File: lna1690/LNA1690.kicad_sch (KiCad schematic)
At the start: 37 parts, among them J1 Screw_Terminal_01x02, J2 Conn_Coaxial, J3 Conn_Coaxial, U1 TQP3M9008, U2 AMS1117-5.0, U3 TA1125A, U4 TQP3M9008, U5 TA1125A, U6 TQP3M9008

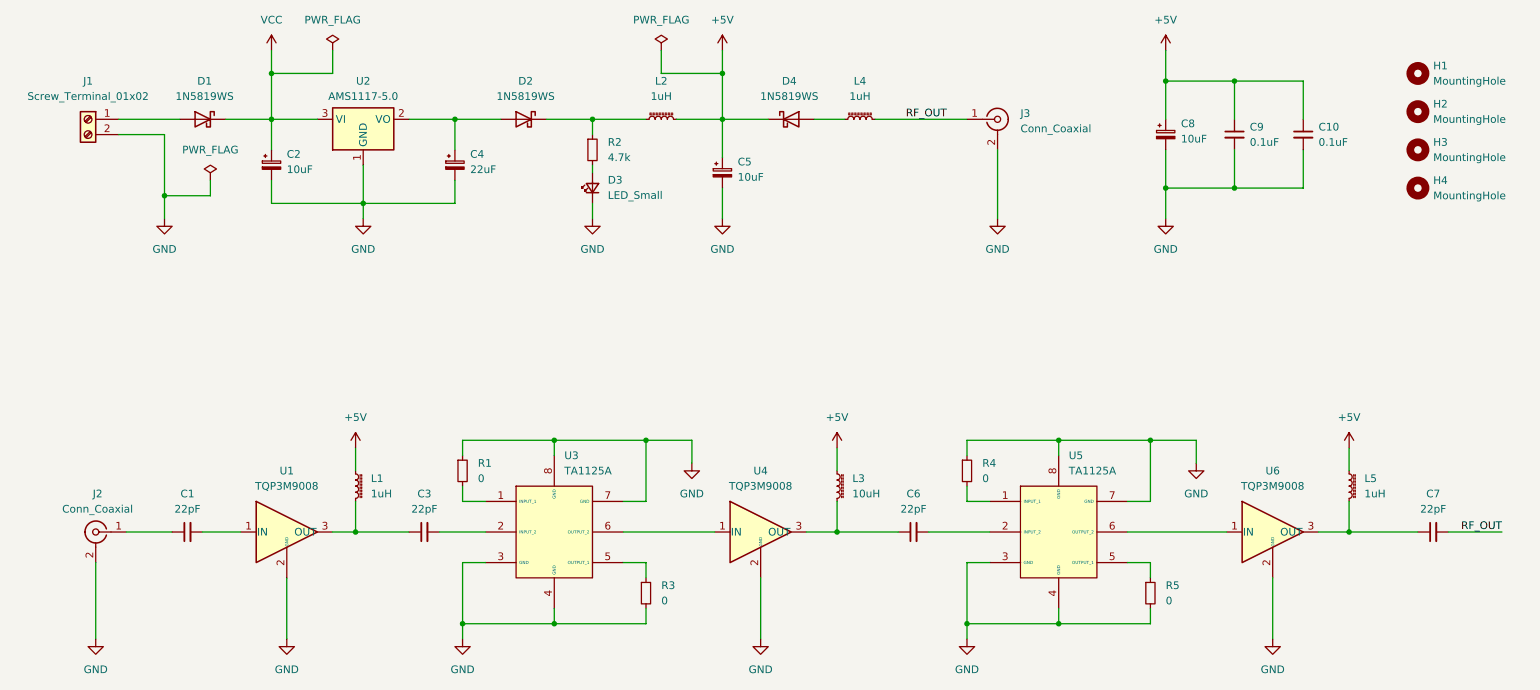
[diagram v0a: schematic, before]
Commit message: Update LNA schematic
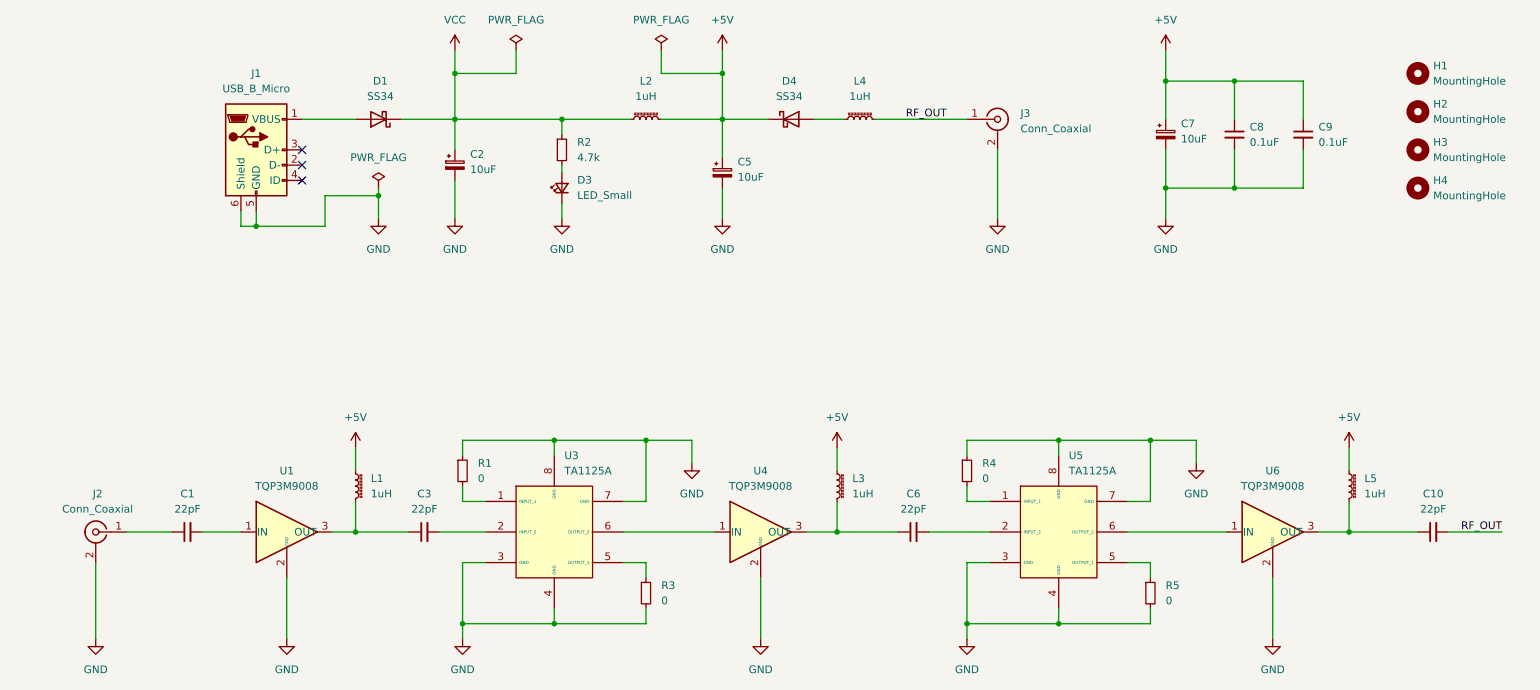
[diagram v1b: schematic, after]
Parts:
- removed C4: 22uF, Capacitor_Tantalum_SMD:CP_EIA-3528-12_Kemet-T, symbol Device:C_Polarized_Small
- removed D1, D2, D4: 1N5819WS, Diode_SMD:D_SOD-323, symbol Diode:1N5819WS
- removed J1: Screw_Terminal_01x02, TerminalBlock:TerminalBlock_bornier-2_P5.08mm, symbol Connector:Screw_Terminal_01x02
- removed U2: AMS1117-5.0, Package_TO_SOT_SMD:SOT-223-3_TabPin2, symbol Regulator_Linear:AMS1117-5.0
- added D1, D4: SS34, Diode_SMD:D_SMA, symbol Diode:SS34
- added J1: USB_B_Micro, Connector_USB:USB_Micro-B_Amphenol_10103594-0001LF_Horizontal, symbol Connector:USB_B_Micro
- L3: value 10uH -> 1uH
- renumbered C7 to C10, C8 to C7, C9 to C8, C10 to C9
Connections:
- net +5V: now also D4.1 (K)
- net GND: now also J1.5 (GND), J1.6 (Shield)
- net VCC: now also L2.1, R2.1, D1.1 (K)
- net at L4.1: now also D4.2 (A)
- new net: D1.2 (A), J1.1 (VBUS)
- no-connect marks 0 -> 3
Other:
- moved on the sheet: C2, D3, L2, R2
